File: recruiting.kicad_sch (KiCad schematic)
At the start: 1 part

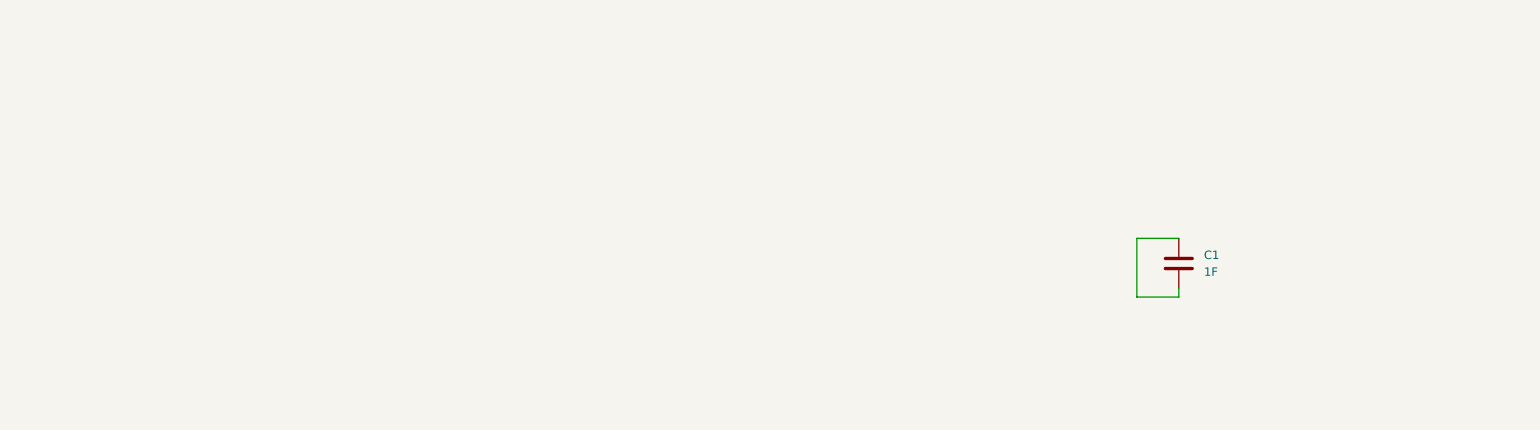
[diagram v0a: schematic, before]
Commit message: Add hierarchical sheet with power monitor
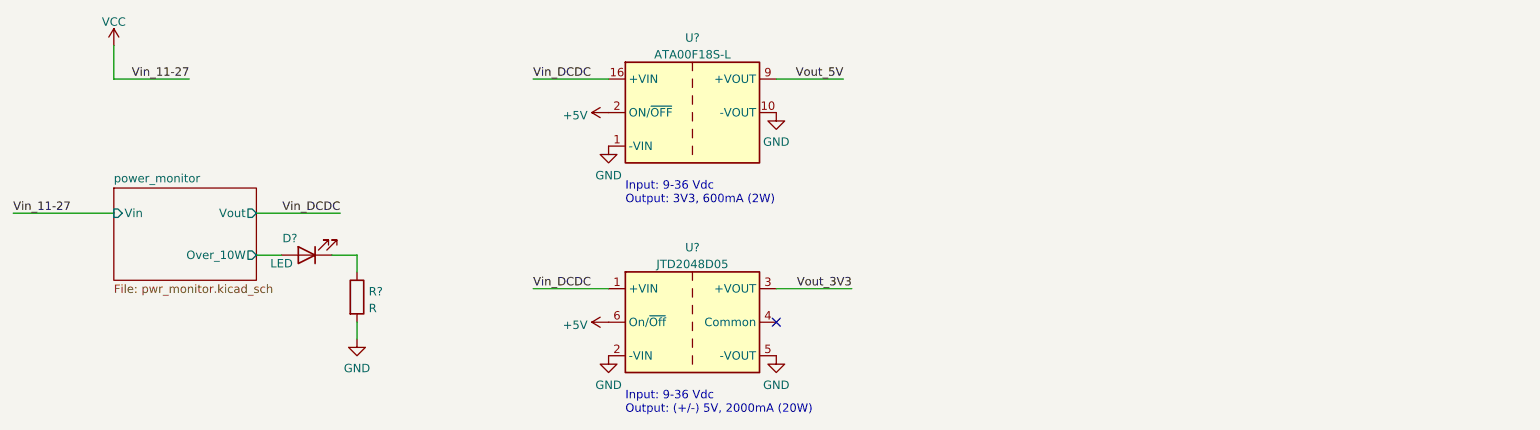
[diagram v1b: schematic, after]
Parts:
- removed C1: 1F, Capacitor_SMD:C_0805_2012Metric, symbol Device:C
- added D?: LED, symbol Device:LED
- added R?: R, symbol Device:R
- added U?: ATA00F18S-L, Converter_DCDC:Converter_DCDC_Artesyn_ATA_SMD, symbol Converter_DCDC:ATA00F18S-L
- added U?: JTD2048D05, Converter_DCDC:Converter_DCDC_XP_POWER_JTDxxxxxxx_THT, symbol Converter_DCDC:JTD2048D05
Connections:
- new net: D?.1 (K), R?.1
- new net +5V: U?.2 (ON/~{OFF}), U?.6 (On/~{Off})
- new net GND: R?.2, U?.1 (-VIN), U?.10 (-VOUT), U?.2 (-VIN), U?.5 (-VOUT)
- new net Vin_DCDC: U?.1 (+VIN), U?.16 (+VIN)
- new net Vout_3V3: U?.3 (+VOUT)
- new net Vout_5V: U?.9 (+VOUT)
- new net power_monitor/Over_10W: D?.2 (A)
- no-connect marks 0 -> 1
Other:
- added sheet power_monitor (pwr_monitor.kicad_sch)
- note added: "Input: 9-36 Vdc Output: (+/-) 5V, 2000mA (20W)"
- note added: "Input: 9-36 Vdc Output: 3V3, 600mA (2W)"

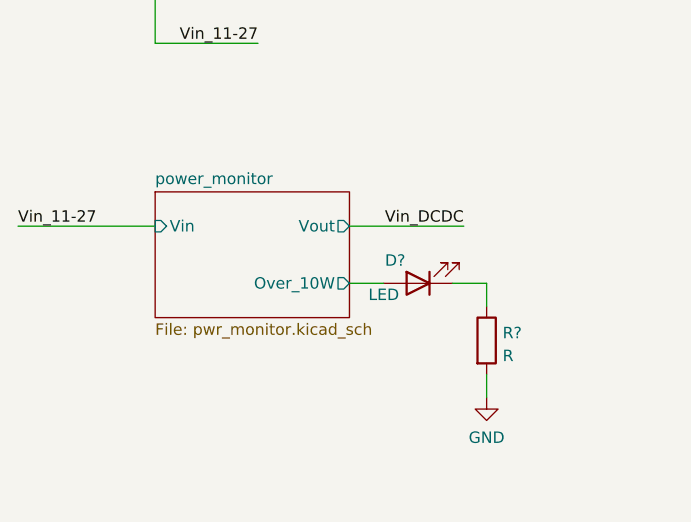
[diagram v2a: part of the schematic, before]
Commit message: Add NE555 to blink LED at 3.5Hz
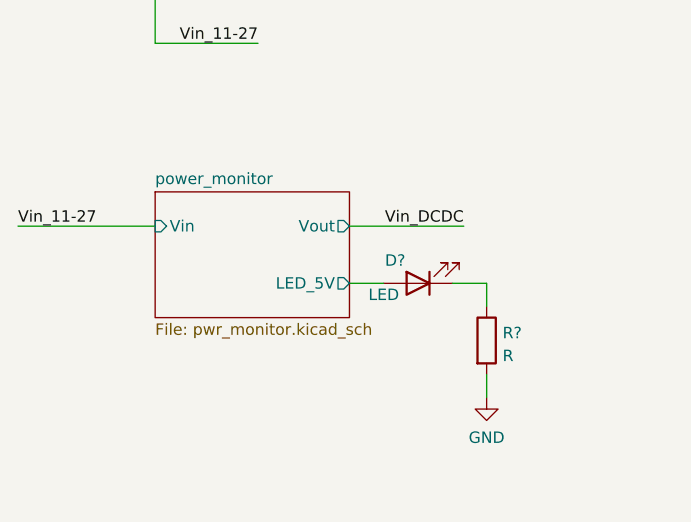
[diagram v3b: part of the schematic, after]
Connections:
- net power_monitor/Over_10W renamed power_monitor/LED_5V
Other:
- sheet power_monitor ports: added LED_5V; removed Over_10W
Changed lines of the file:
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@@
       (effects (font (size 1.27 1.27)) (justify left))
     )
-    (pin "Over_10W" output (at 59.69 124.46 0)
+    (pin "Vout" output (at 59.69 118.11 0)
       (effects (font (size 1.27 1.27)) (justify right))
     )
-    (pin "Vout" output (at 59.69 118.11 0)
+    (pin "LED_5V" output (at 59.69 124.46 0)
       (effects (font (size 1.27 1.27)) (justify right))
     )
@@
   )
   (symbol_instances
+    (path "/7f2f48d1-9a93-4c33-8b0a-340d492711ab/123f9bd7-b417-48c1-a3bd-643d0259a1d8"
+      (reference "#PWR?") (unit 1) (value "GND") (footprint "")
+    )
     (path "/292b3c4b-430f-4d2d-ae90-e3215e708635"
       (reference "#PWR?") (unit 1) (value "+5V") (footprint "")
     )
     (path "/306a509e-50bd-44af-bfcf-f9a97fc2db20"
+      (reference "#PWR?") (unit 1) (value "+5V") (footprint "")
+    )
+    (path "/7f2f48d1-9a93-4c33-8b0a-340d492711ab/5fc5051b-98a7-4d88-8294-669ee836a434"
       (reference "#PWR?") (unit 1) (value "+5V") (footprint "")
     )
@@
       (reference "#PWR?") (unit 1) (value "GND") (footprint "")
     )
+    (path "/7f2f48d1-9a93-4c33-8b0a-340d492711ab/82e7c523-3cb1-493d-ac97-b17655d4401e"
+      (reference "#PWR?") (unit 1) (value "GND") (footprint "")
+    )
     (path "/8ad29919-1b9d-4601-824e-ca02695fe1aa"
+      (reference "#PWR?") (unit 1) (value "GND") (footprint "")
+    )
+    (path "/7f2f48d1-9a93-4c33-8b0a-340d492711ab/923371cf-3152-4711-8cdc-610f94ad672a"
       (reference "#PWR?") (unit 1) (value "GND") (footprint "")
     )
@@
       (reference "#PWR?") (unit 1) (value "VCC") (footprint "")
     )
+    (path "/7f2f48d1-9a93-4c33-8b0a-340d492711ab/3dab94da-78c1-4b60-b17a-27168d8560b6"
+      (reference "C?") (unit 1) (value "2u") (footprint "")
+    )
+    (path "/7f2f48d1-9a93-4c33-8b0a-340d492711ab/c3ef91fc-5db5-4183-9b06-dab0bcba96df"
+      (reference "C?") (unit 1) (value "100n") (footprint "")
+    )
     (path "/5deeffbc-8794-484a-b2a5-e3cc590e7a88"
       (reference "D?") (unit 1) (value "LED") (footprint "")
@@
     (path "/7f2f48d1-9a93-4c33-8b0a-340d492711ab/1e2fc46d-e776-4dc1-9536-d4f0e74d01c3"
       (reference "R?") (unit 1) (value "7.5k") (footprint "")
+    )
+    (path "/7f2f48d1-9a93-4c33-8b0a-340d492711ab/53dde44d-8874-4f48-b115-15c8cc3b3ae2"
+      (reference "R?") (unit 1) (value "100k") (footprint "")
+    )
+    (path "/7f2f48d1-9a93-4c33-8b0a-340d492711ab/563e3349-e5e5-4008-9bec-351c0aefd24a"
+      (reference "R?") (unit 1) (value "1k") (footprint "")
     )
     (path "/7f2f48d1-9a93-4c33-8b0a-340d492711ab/692a3bcf-0de2-4486-acae-c61e8e3909df"
@@
       (reference "U?") (unit 1) (value "LM741") (footprint "")
     )
+    (path "/7f2f48d1-9a93-4c33-8b0a-340d492711ab/6951b5f1-5326-42c8-b023-e331ee710437"
+      (reference "U?") (unit 1) (value "NE555P") (footprint "Package_DIP:DIP-8_W7.62mm")
+    )
     (path "/9f55fb12-5697-4d82-b926-9f18bd01e6e4"

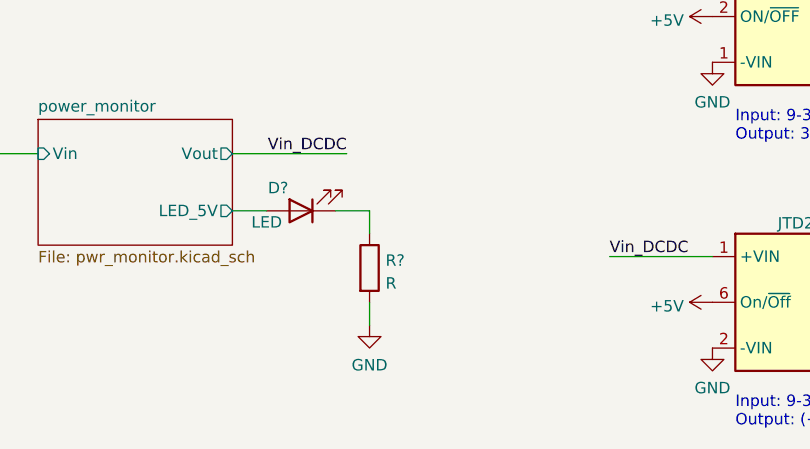
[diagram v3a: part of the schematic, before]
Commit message: Finish power monitor
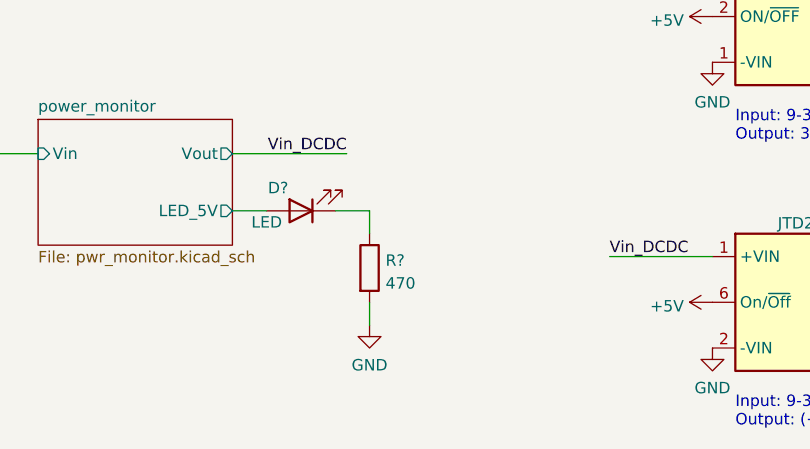
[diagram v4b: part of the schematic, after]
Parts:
- R?: value R -> 470
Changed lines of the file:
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@@
       (effects (font (size 1.27 1.27)) (justify left))
     )
-    (property "Value" "R" (id 1) (at 76.708 132.5122 0)
+    (property "Value" "470" (id 1) (at 76.708 132.5122 0)
       (effects (font (size 1.27 1.27)) (justify left))
     )
@@
     )
     (path "/aa344f91-1f3b-4c24-9a52-fc60512b7222"
-      (reference "R?") (unit 1) (value "R") (footprint "")
+      (reference "R?") (unit 1) (value "470") (footprint "")
     )
     (path "/7f2f48d1-9a93-4c33-8b0a-340d492711ab/3aaefd01-c336-4933-8f29-96bda986752e"

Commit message: Create PCB
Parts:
- added H1, H2, H3: MountingHole, MountingHole:MountingHole_2mm, symbol Mechanical:MountingHole
- added J1, J2, J3: Screw_Terminal_01x02, TerminalBlock_4Ucon:TerminalBlock_4Ucon_1x02_P3.50mm_Horizontal, symbol Connector:Screw_Terminal_01x02
- D1: renamed from D?; footprint (none) -> LED_SMD:LED_1206_3216Metric
- R1: renamed from R?; footprint (none) -> Resistor_SMD:R_1206_3216Metric
- gave numbers to parts that had none: 2
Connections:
- net Vout_5V is gone; now on net +5V: U1.9 (+VOUT)
- net +5V: now also J2.1 (Pin_1)
- net GND: now also J1.2 (Pin_2), J2.2 (Pin_2), J3.2 (Pin_2)
- net Vout_3V3: now also J3.1 (Pin_1)
- new net Vin_11-27: J1.1 (Pin_1)
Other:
- title: Template -> Enzomma
